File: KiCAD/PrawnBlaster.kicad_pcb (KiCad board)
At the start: 2 copper layers, 160 x 100 mm, 30 parts, among them J1 Conn_02x06_Odd_Even, J10 Conn_01x20_Male, J6 C64AC, J8 Conn_01x20_Male, J9 Conn_01x03_Male, Q1 DMP6023LE, U1 Pico, U2 SN74LV1T34DBV, U3 78L05, U4 74ABT245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

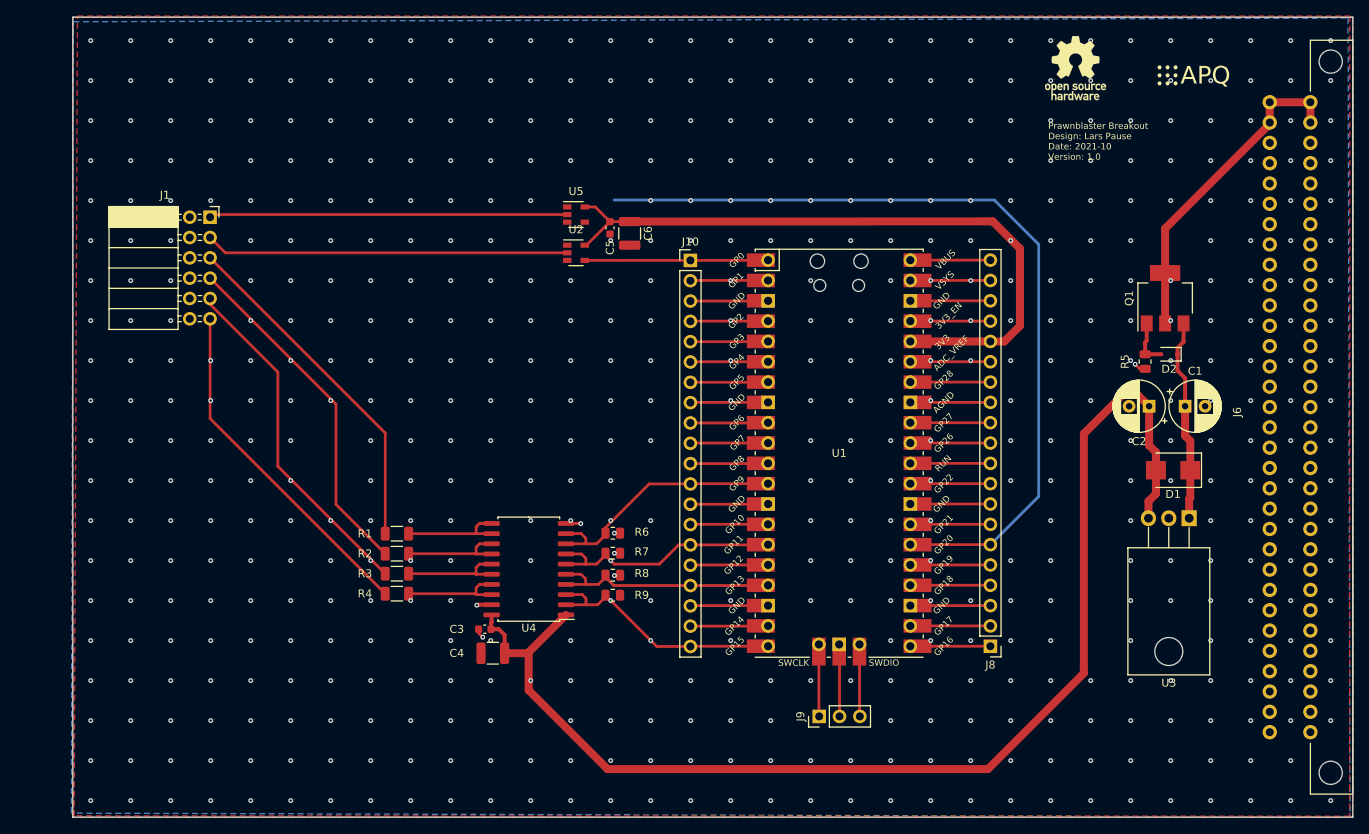
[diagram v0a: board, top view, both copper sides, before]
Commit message: Add USB-isolator plus extra power supply; move parts
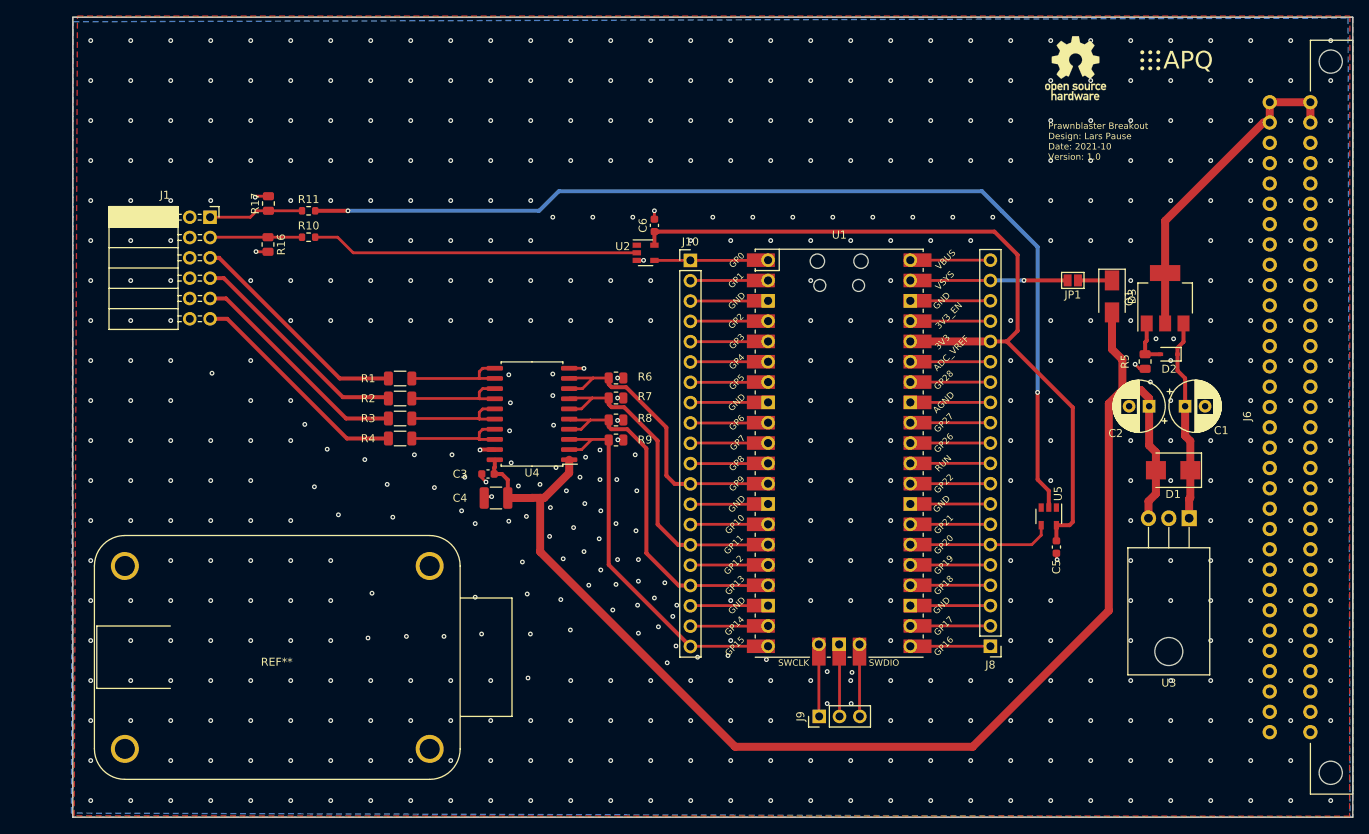
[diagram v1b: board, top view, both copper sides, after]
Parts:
- added D3: D_Schottky, Diode_SMD:D_SMA, F.Cu at (170.9, 82.9)
- added JP1: Jumper_NO_Small, Jumper:SolderJumper-2_P1.3mm_Open_Pad1.0x1.5mm, F.Cu at (166.0, 80.9)
- added R10: 500, Resistor_SMD:R_0603_1608Metric, F.Cu at (70.5, 75.5)
- added R11: 500, Resistor_SMD:R_0603_1608Metric, F.Cu at (70.5, 72.2)
- added R16: 47k, Resistor_SMD:R_0805_2012Metric, F.Cu at (65.4, 76.4)
- added R17: 47k, Resistor_SMD:R_0805_2012Metric, F.Cu at (65.5, 71.3)
- added REF**: usb_isolator, adafruit:usb_isolator, F.Cu at (67.0, 128.0)
- C6: value 10u -> 100n; footprint Capacitor_SMD:C_1210_3225Metric -> Capacitor_SMD:C_0603_1608Metric
- U2, U5: value SN74LV1T34DBV -> 74LVC1G07
- moved U5 70.1 mm to (163.0, 110.4), turned to 270 degrees
- moved C5 68.6 mm to (163.9, 114.2)
- moved C3 19.4 mm to (92.9, 105.1)
- moved C4 19.4 mm to (93.9, 108.1)
- moved R6 19.4 mm to (108.9, 93.1)
- moved R7 19.4 mm to (108.9, 95.6)
- moved R8 19.4 mm to (108.9, 98.3)
- moved R9 19.4 mm to (108.9, 100.8)
- moved U4 19.4 mm to (98.4, 97.6)
- moved R1 19.4 mm to (81.9, 93.2)
- moved R2 19.4 mm to (81.9, 95.7)
- moved R3 19.4 mm to (81.9, 98.2)
- moved R4 19.4 mm to (81.9, 100.7)
- moved U2 8.70 mm to (112.6, 77.5)
- moved C6 3.25 mm to (113.7, 74.0), turned to 90 degrees
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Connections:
- net /Output Buffer/Vcc renamed /Output Buffer/Vcc_5V
- net Net-(C5-Pad1) renamed 3_3V_Pico
- U2 pad 2: Net-(J1-Pad3) -> Net-(R10-Pad2)
- U5 pad 2: Net-(J1-Pad1) -> Net-(R11-Pad2)
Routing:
- net Net-(R11-Pad2): track 0.00 -> 127.4 mm, vias 0 -> 2
- net Net-(J8-Pad6): track 105.4 -> 18.1 mm, vias 9 -> 0
- net Net-(R10-Pad2): track 0.00 -> 41.0 mm
- net Net-(J1-Pad3): track 45.4 -> 11.5 mm
- net Net-(J1-Pad1): track 44.8 -> 11.8 mm
- net 3_3V_Pico: track 85.1 -> 101.9 mm, vias 1 -> 0
- net /Output Buffer/A0: track 32.0 -> 48.1 mm, vias 2 -> 0
- net /Output Buffer/Vcc_5V: track 154.4 -> 169.7 mm, vias 1 -> 0
- net Net-(J1-Pad5): track 43.5 -> 28.5 mm
- net Net-(J1-Pad7): track 43.5 -> 28.5 mm, vias 3 -> 0
- net Net-(J1-Pad9): track 43.5 -> 28.5 mm, vias 3 -> 0
- net Net-(J1-Pad11): track 43.4 -> 28.5 mm, vias 2 -> 0
- net /Output Buffer/A1: track 30.0 -> 44.8 mm
- net /Output Buffer/A2: track 31.1 -> 42.6 mm, vias 1 -> 0
- net Net-(J8-Pad19): track 10.0 -> 19.7 mm, vias 2 -> 1
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
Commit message: Reduce GND-connections to pico to 1
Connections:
- J10 pad 13: GND -> Net-(J10-Pad13)
- J10 pad 18: GND -> Net-(J10-Pad18)
- J10 pad 3: GND -> Net-(J10-Pad3)
- J10 pad 8: GND -> Net-(J10-Pad8)
- J8 pad 3: GND -> Net-(J8-Pad3)
- J8 pad 8: GND -> Net-(J8-Pad8)
- J9 pad 2: GND -> Net-(J9-Pad2)
- U1 pad 13: GND -> Net-(J10-Pad13)
- U1 pad 18: GND -> Net-(J10-Pad18)
- U1 pad 23: GND -> Net-(J8-Pad3)
- U1 pad 28: GND -> Net-(J8-Pad8)
- U1 pad 3: GND -> Net-(J10-Pad3)
- U1 pad 42: GND -> Net-(J9-Pad2)
- U1 pad 8: GND -> Net-(J10-Pad8)
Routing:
- net GND: track 93.5 -> 25.6 mm, vias 574 -> 573
- net Net-(J8-Pad8): track 0.00 -> 10.0 mm
- net Net-(J8-Pad3): track 0.00 -> 10.0 mm
- net Net-(J10-Pad8): track 0.00 -> 9.72 mm
- net Net-(J10-Pad3): track 0.00 -> 9.72 mm
- net Net-(J10-Pad18): track 0.00 -> 9.72 mm
- net Net-(J10-Pad13): track 0.00 -> 9.72 mm
- net Net-(J9-Pad2): track 0.00 -> 9.02 mm
- net (no net): vias 0 -> 1

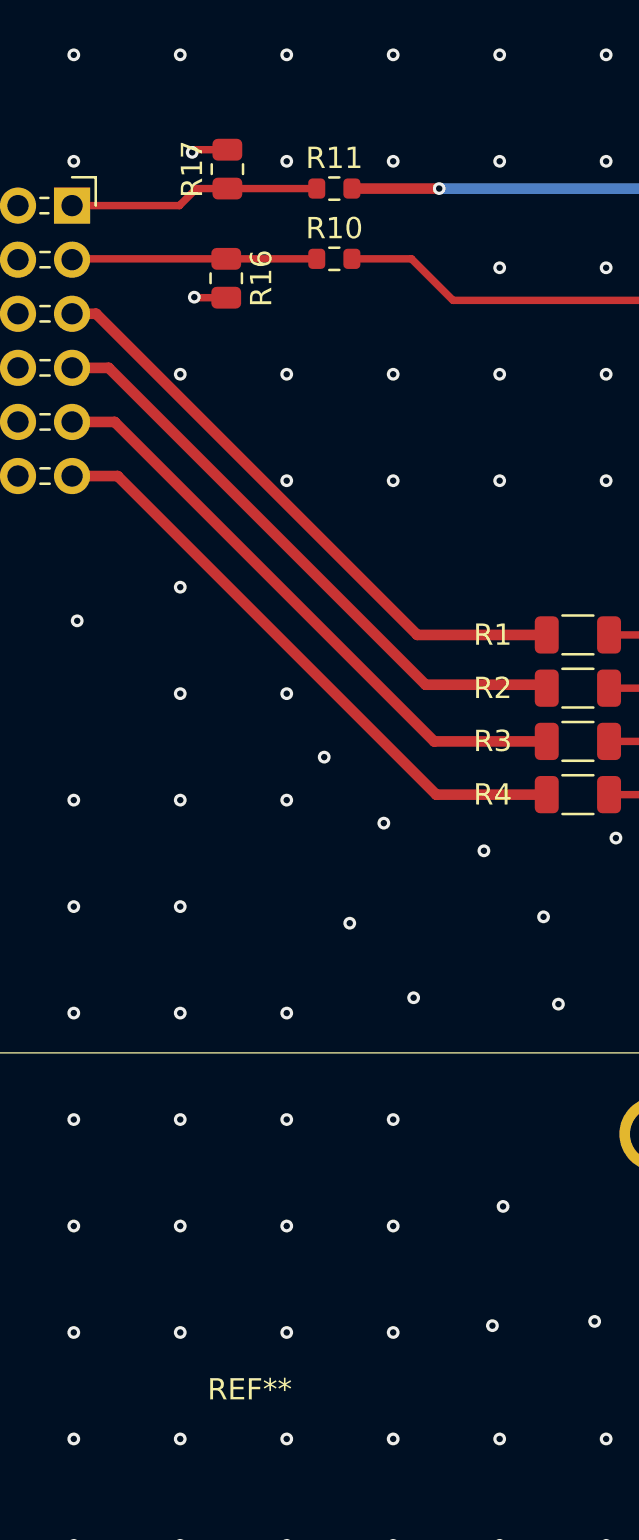
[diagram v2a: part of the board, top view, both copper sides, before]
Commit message: Update non-available parts and add missing usb isolator to bom
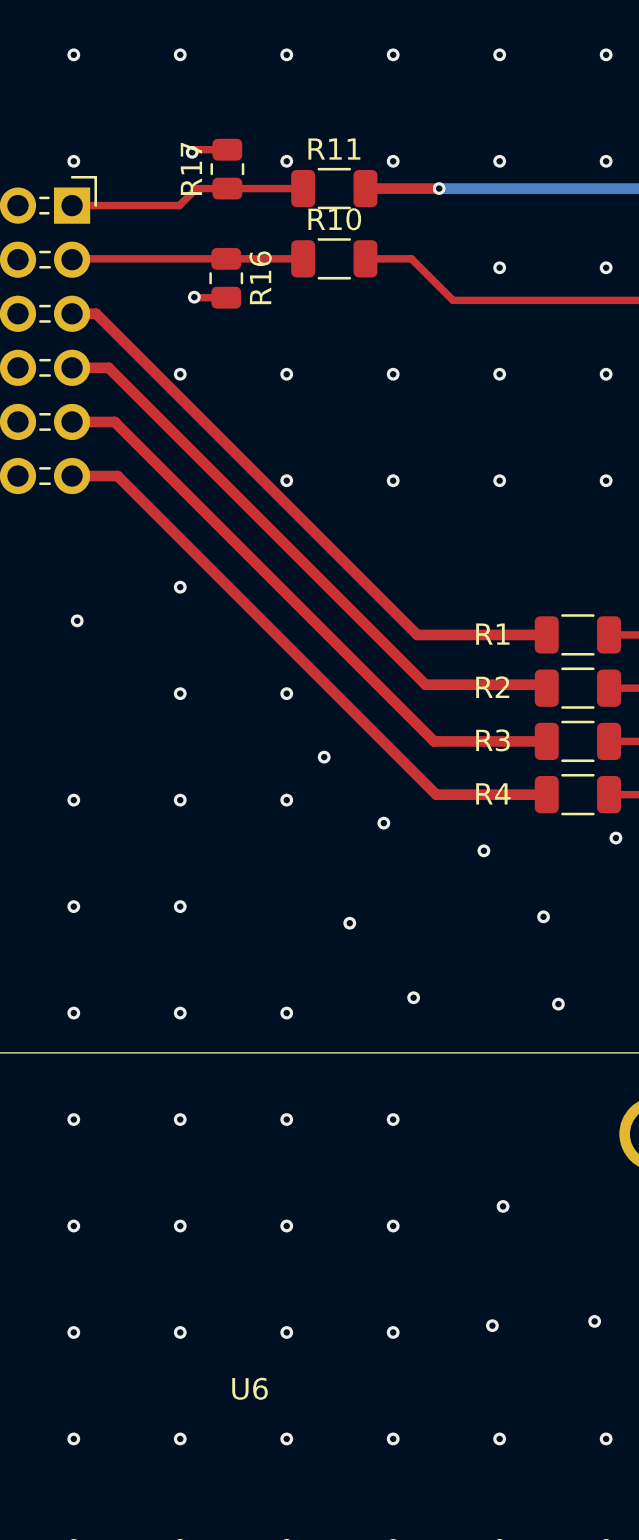
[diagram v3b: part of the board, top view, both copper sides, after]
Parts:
- removed REF**: usb_isolator, adafruit:usb_isolator
- added U6: adafruit_usb_isolator, adafruit:usb_isolator, F.Cu at (67.0, 128.0)
- R10, R11: footprint Resistor_SMD:R_0603_1608Metric -> Resistor_SMD:R_1206_3216Metric
- U3: value 78L05 -> 7805
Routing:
- net Net-(R11-Pad2): track 127.4 -> 126.7 mm
- net Net-(R10-Pad2): track 41.0 -> 40.4 mm
- net Net-(J1-Pad3): track 11.5 -> 10.9 mm
- net Net-(J1-Pad1): track 11.8 -> 11.2 mm
- net GND: vias 573 -> 571
- net (no net): vias 1 -> 3

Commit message: Connected via under R9
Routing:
- net GND: track 25.6 -> 26.3 mm

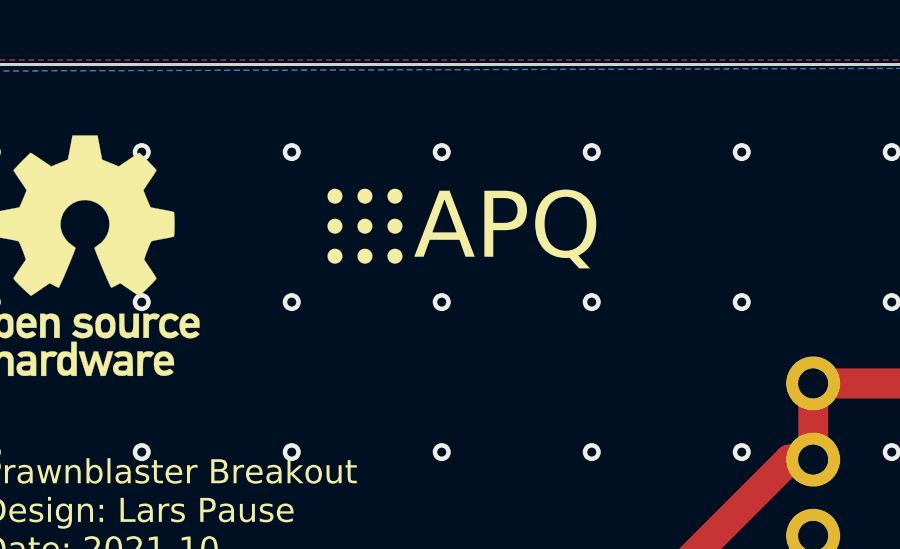
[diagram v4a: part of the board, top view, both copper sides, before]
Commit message: Update Logo position
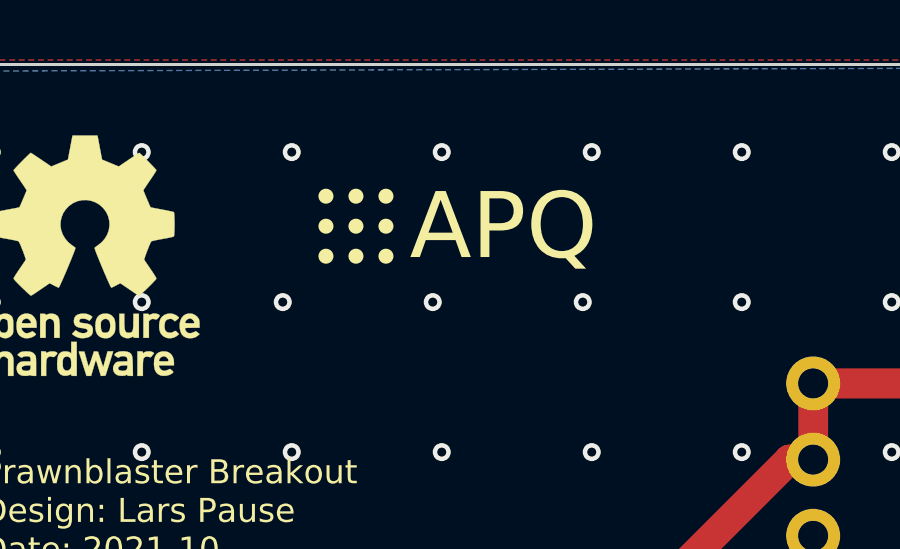
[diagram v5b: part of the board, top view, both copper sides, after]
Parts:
- moved LOGO1 0.30 mm to (174.4, 52.4)

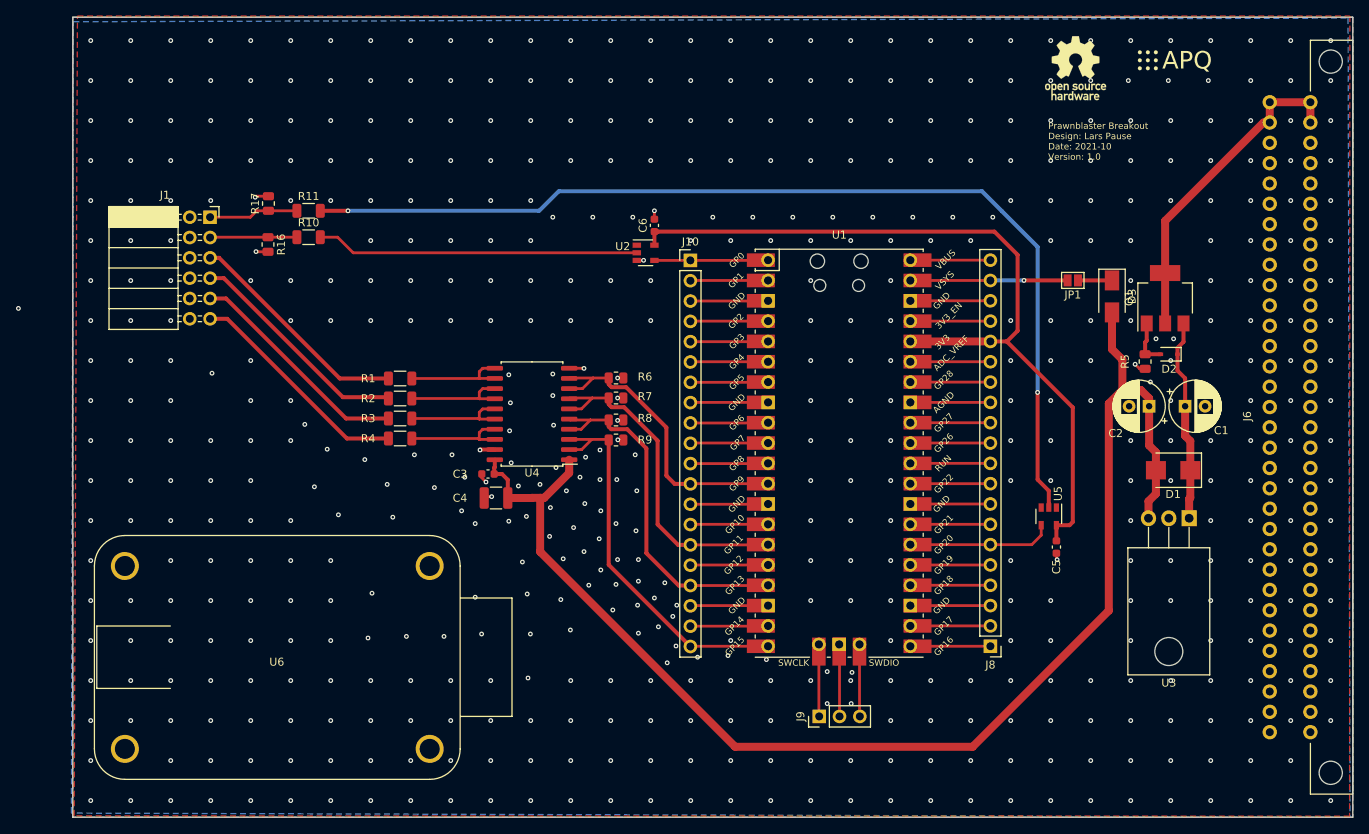
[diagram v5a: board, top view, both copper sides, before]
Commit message: Adjust PCB-Layout
Move Adafruit and Frontpanel connector closer to edge; Untangle Q1 and D3 Silkscreen
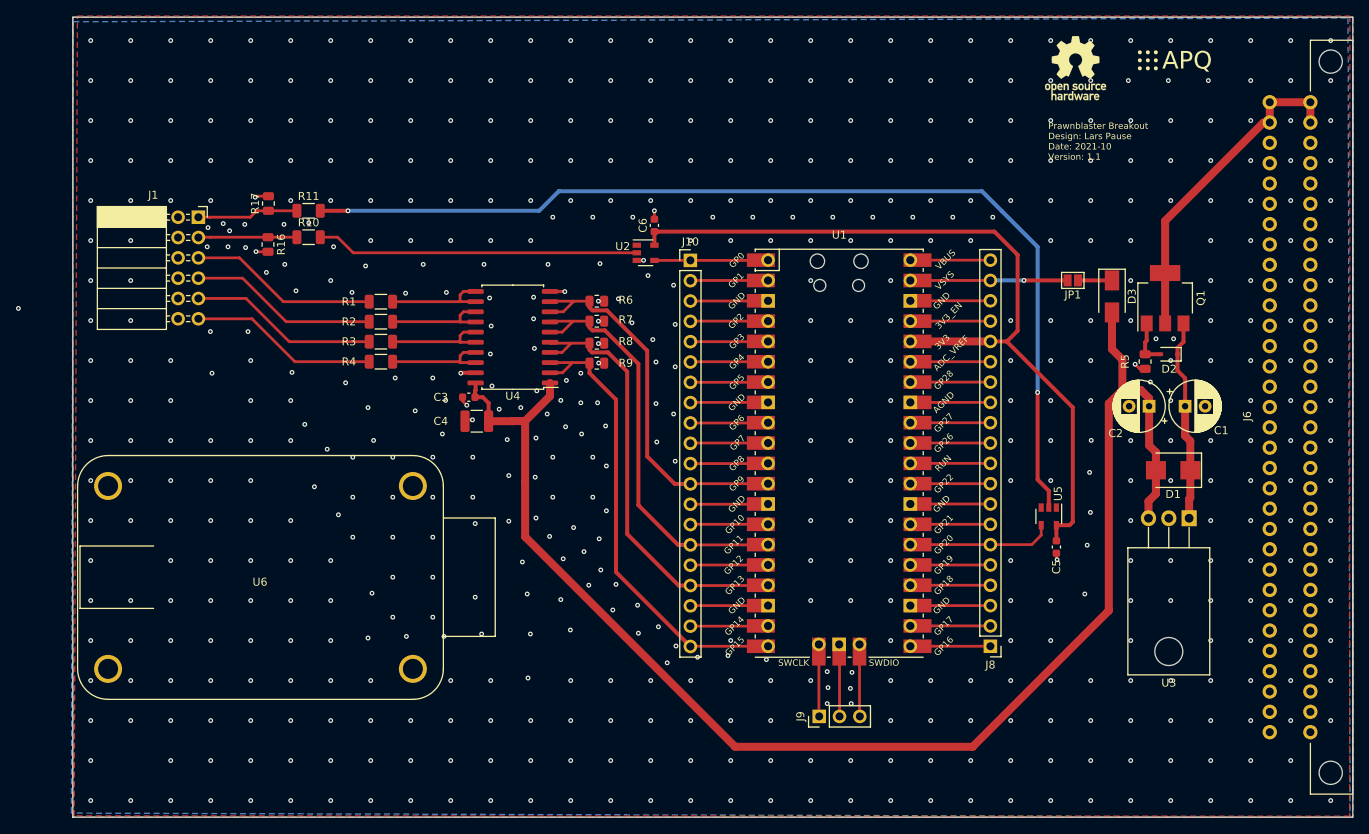
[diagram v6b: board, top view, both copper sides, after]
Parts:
- U2: value 74LVC1G07 -> 74LVC1G17
- moved U6 10.2 mm to (64.9, 118.0)
- moved R1 9.90 mm to (79.5, 83.6)
- moved R2 9.90 mm to (79.5, 86.1)
- moved R3 9.90 mm to (79.5, 88.6)
- moved R4 9.90 mm to (79.5, 91.1)
- moved C3 9.90 mm to (90.5, 95.5)
- moved C4 9.90 mm to (91.5, 98.5)
- moved R6 9.90 mm to (106.5, 83.5)
- moved R7 9.90 mm to (106.5, 86.0)
- moved R8 9.90 mm to (106.5, 88.8)
- moved R9 9.90 mm to (106.5, 91.2)
- moved U4 9.90 mm to (96.0, 88.0)
- moved J1 1.46 mm to (56.7, 73.0)
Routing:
- net /Output Buffer/A0: track 48.1 -> 58.7 mm
- net /Output Buffer/A3: track 37.9 -> 48.5 mm
- net /Output Buffer/A1: track 44.8 -> 55.4 mm
- net /Output Buffer/A2: track 42.6 -> 53.2 mm
- net /Output Buffer/Vcc_5V: track 169.7 -> 180.1 mm
- net Net-(J1-Pad7): track 28.5 -> 23.6 mm
- net Net-(J1-Pad9): track 28.5 -> 23.6 mm
- net Net-(J1-Pad11): track 28.5 -> 23.6 mm
- net Net-(J1-Pad5): track 28.5 -> 23.6 mm
- net Net-(J1-Pad3): track 10.9 -> 12.3 mm
- net Net-(J1-Pad1): track 11.2 -> 12.6 mm
- net GND: vias 571 -> 604
- net (no net): vias 3 -> 13
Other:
- board text added: "Prawnblaster Breakout Design: Lars Pause Date: 2021-10 Version: 1.1"
- board text removed: "Prawnblaster Breakout Design: Lars Pause Date: 2021-10 Version: 1.0"
